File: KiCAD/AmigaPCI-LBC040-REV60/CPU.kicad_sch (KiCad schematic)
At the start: 29 parts, among them J100 SNOOP, J101 MMU/CACHE, U112 74LVC244, U200 MC68040, U203 74LVC245

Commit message: Add JLCPCB part numbers to KiCAD schematic.
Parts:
- C139, C200, C201, C202, C203, C204, C205, C206, C207, C208, C209, C210, C211, C212, C214, C247: LCSC (none) -> C14663
- J100, J101: LCSC (none) -> C2451133
- R100, R101, R102, R103: LCSC (none) -> C25804
- R104, R111: LCSC (none) -> C23345
- R105, R110: LCSC (none) -> C13167
- U112: LCSC (none) -> C7668
- U203: LCSC (none) -> C7848

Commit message: Update 2x2 Pin Header Part Numbers
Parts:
- J100, J101: LCSC C2451133 -> C66690
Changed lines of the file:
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@@
 			)
 		)
-		(property "LCSC" "C2451133"
+		(property "LCSC" "C66690"
 			(at 128.27 118.11 0)
 			(effects
@@
 			)
 		)
-		(property "LCSC" "C2451133"
+		(property "LCSC" "C66690"
 			(at 139.7 165.1 0)
 			(effects

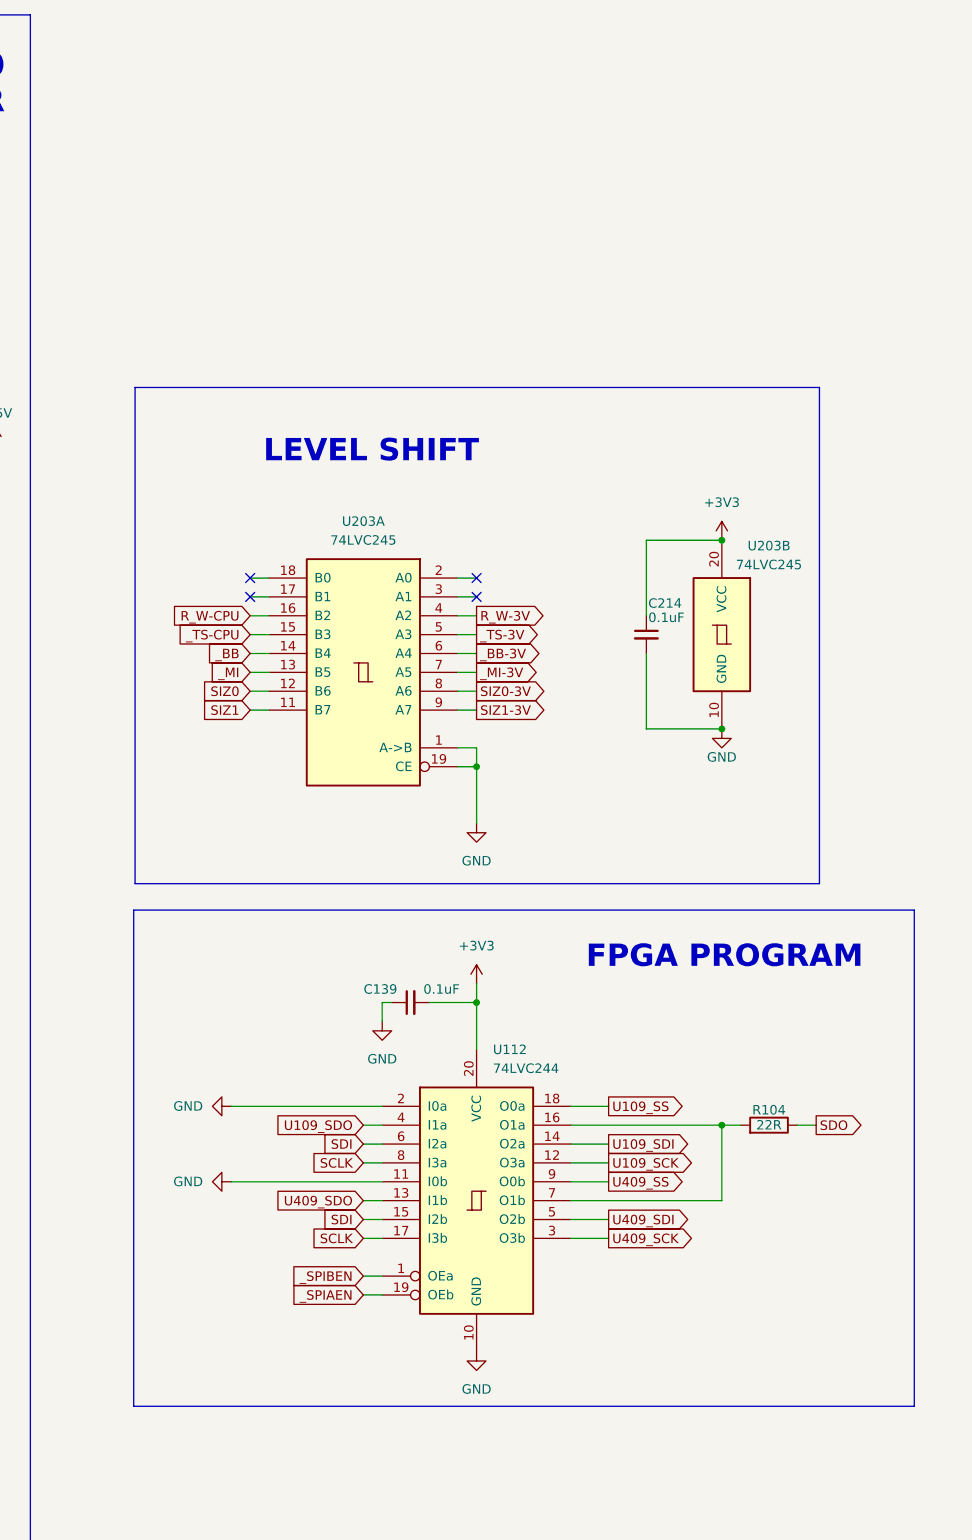
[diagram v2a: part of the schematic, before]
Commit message: Add part number for DIN41612 connector.
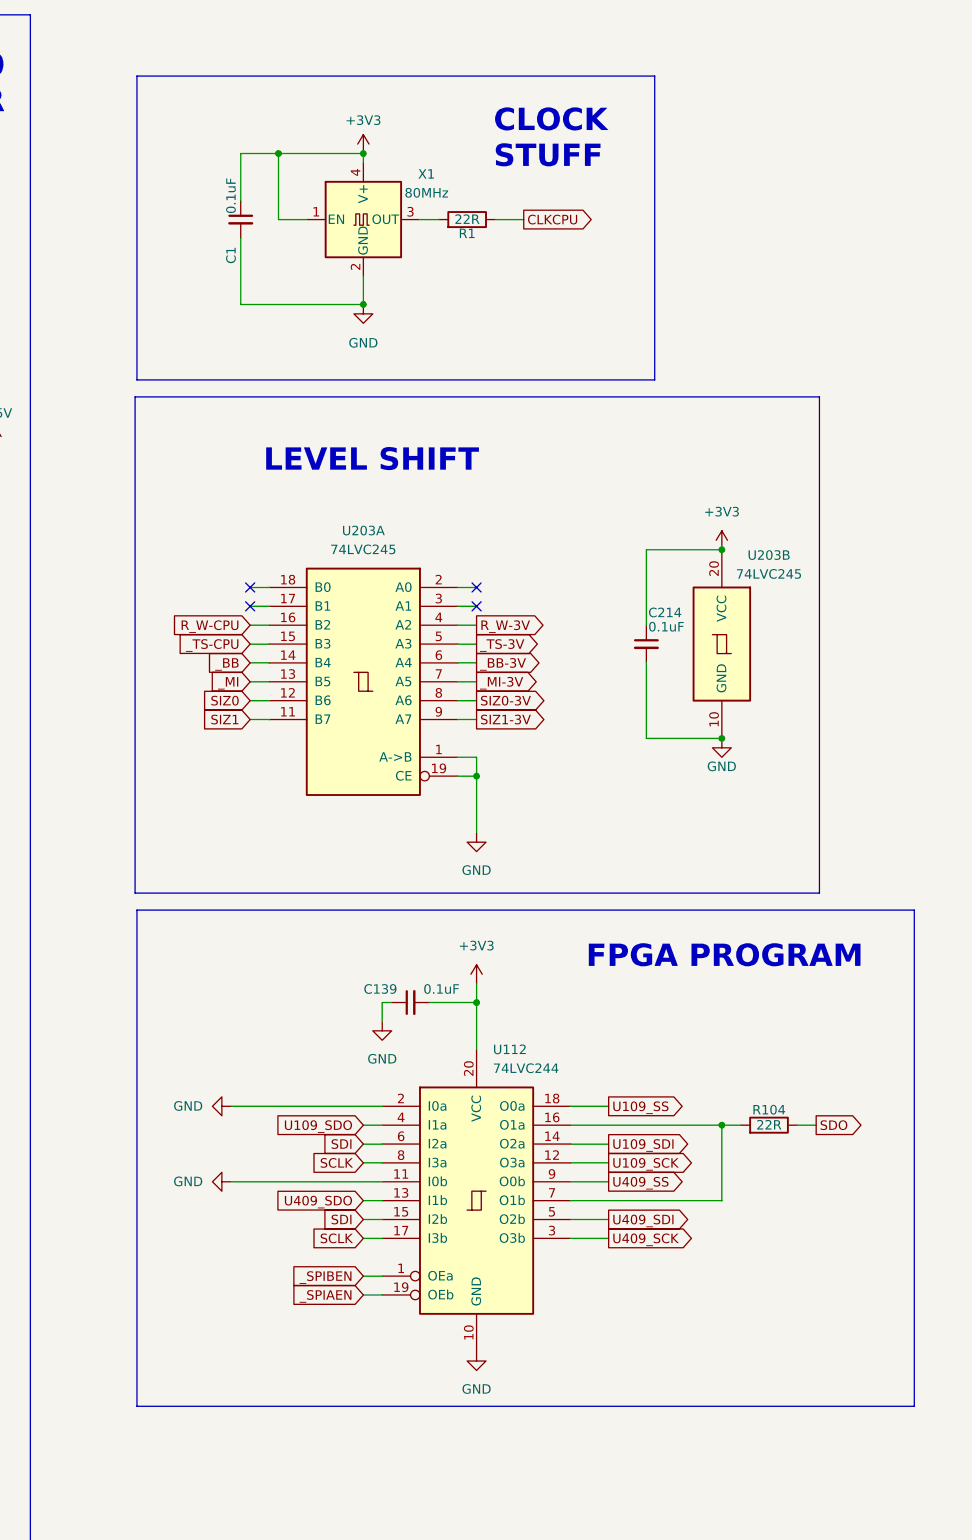
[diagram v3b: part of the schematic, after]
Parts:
- added C1: 0.1uF, Capacitor_SMD:C_0603_1608Metric, symbol Device:C_Small
- added R1: 22R, Resistor_SMD:R_0603_1608Metric, symbol Device:R
- added X1: 80MHz, Oscillator:Oscillator_SMD_ECS_2520MV-xxx-xx-4Pin_2.5x2.0mm, symbol Oscillator:XO32
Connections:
- net +3V3: now also C1.1, X1.1 (EN), X1.4 (V+)
- net GND: now also C1.2, X1.2 (GND)
- new net: R1.2, X1.3 (OUT)
- new net CLKCPU: R1.1
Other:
- note added: "CLOCK STUFF"
- moved on the sheet: C214, U203A, U203B
